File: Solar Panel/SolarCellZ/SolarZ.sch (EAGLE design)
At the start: 34 parts, among them X1 BU-SMA-V

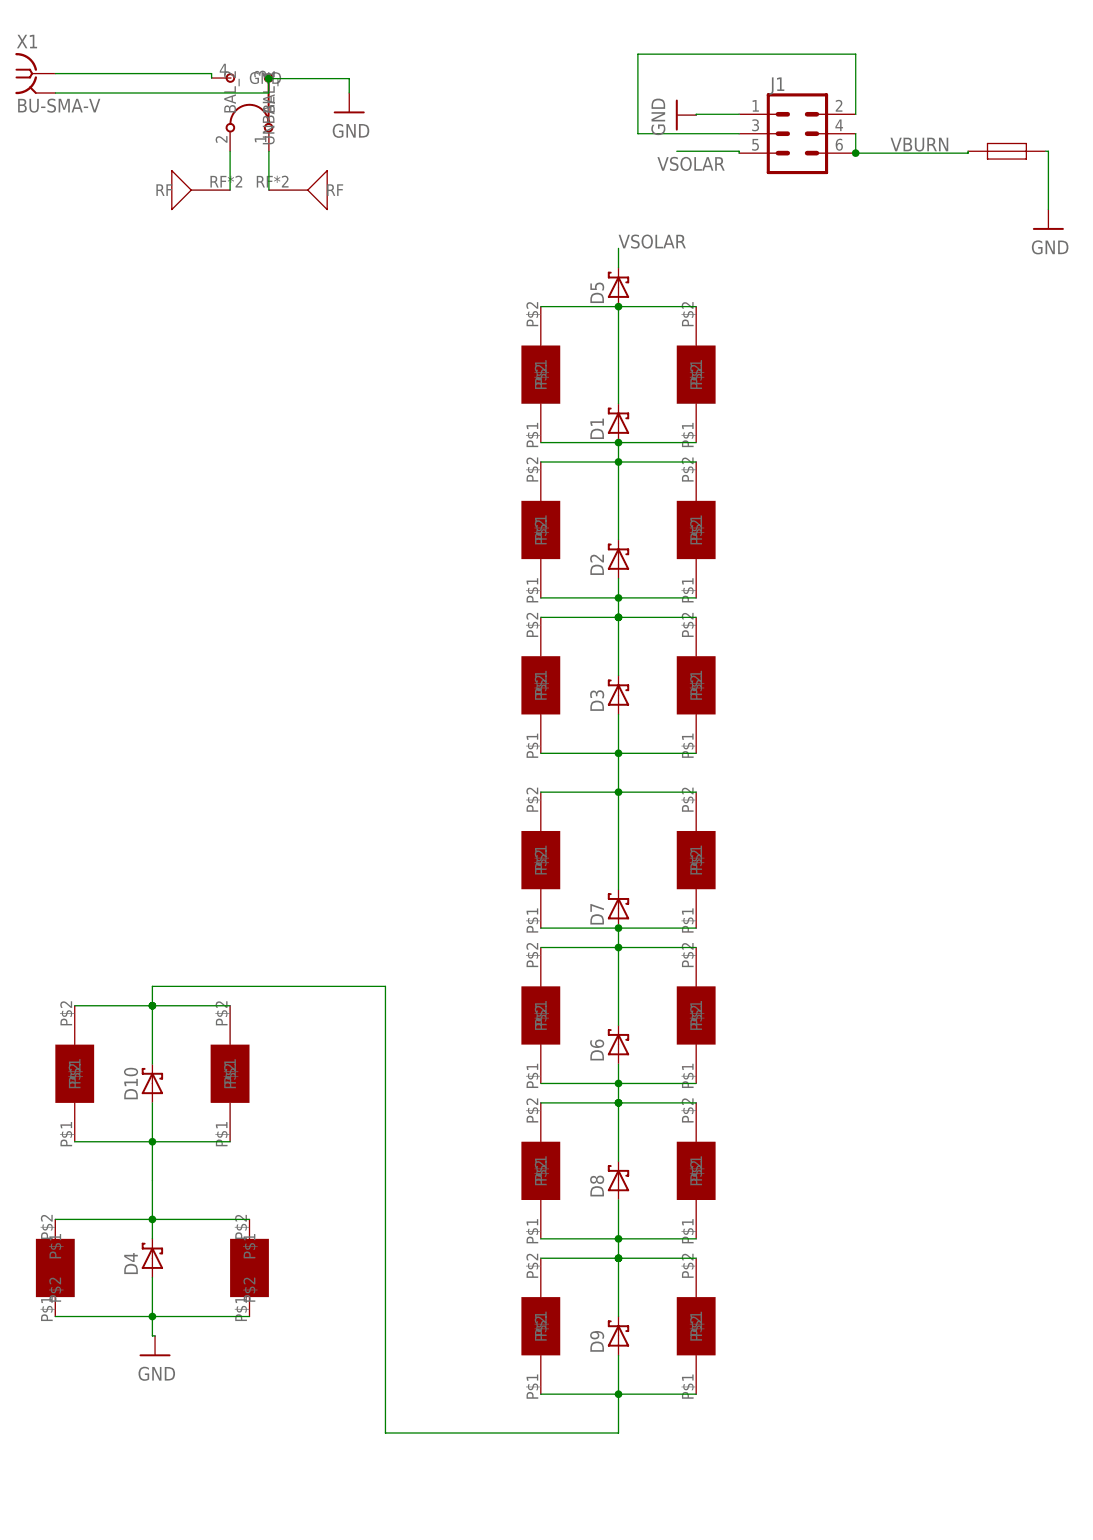
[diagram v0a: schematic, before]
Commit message: Routing on draft Z panel - dimensions need to be confirmed
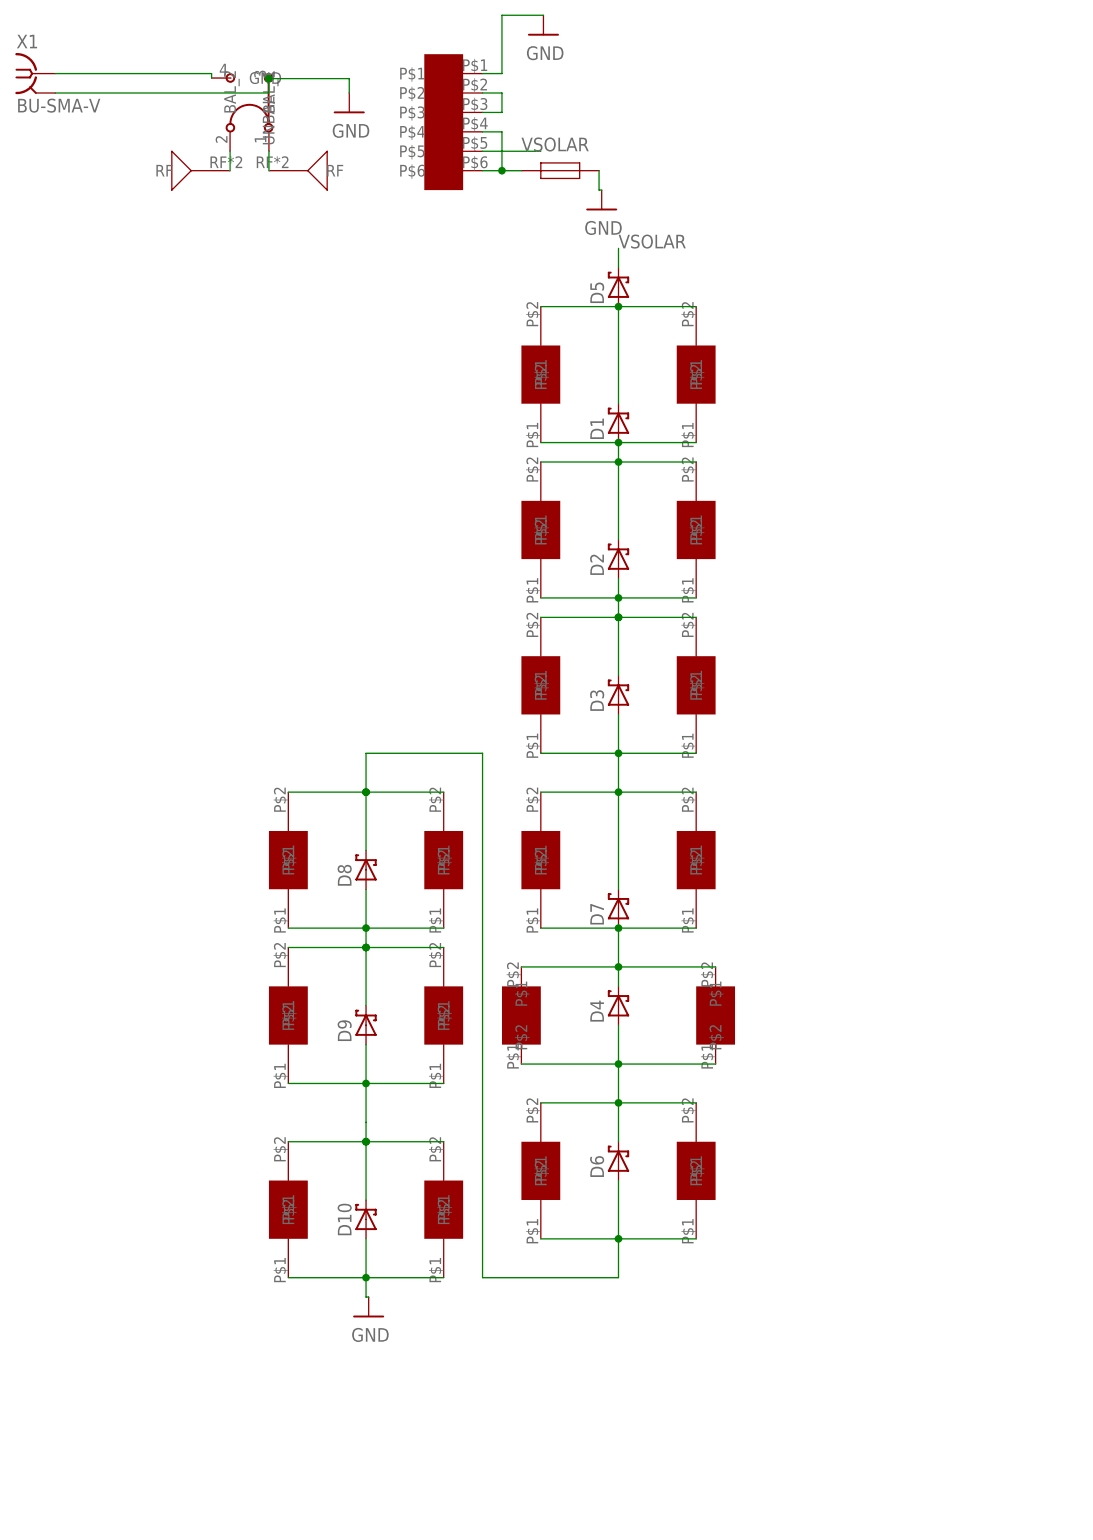
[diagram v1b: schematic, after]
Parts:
- removed F1: (no value), pandasat:BURN_TERM
- removed J1: (no value), pandasat:CONN_03X22X3_SILK_MALE_PTH
- added F2: (no value), pandasat:BURN_TERM
- added U$4: M20-8760342, Solar:M20-8760342
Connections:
- removed net N$1 (its old number): J1.2, J1.3
- removed net N$13: 17.P$1, 18.P$1, D10.POS
- removed net N$4: U$1.BAL_2, U$2.RF
- removed net N$5: U$1.BAL_1, U$3.RF
- removed net VBURN: F1.1, J1.4, J1.6
- new net N$16: F2.1, U$4.P$4, U$4.P$6
- new net N$8: U$4.P$2, U$4.P$3
- new net N$9: 10.P$1, 11.P$1, 6.P$2, 7.P$2, D4.NEG, D7.POS
- new net RF_P: U$1.BAL_2, U$3.RF
- net GND: now also 17.P$1, 18.P$1, D10.POS, F2.2, U$4.P$1; no longer 6.P$1, 7.P$1, D4.POS, F1.2, J1.1
- net N$11: now also 6.P$1, 7.P$1, D4.POS; no longer 10.P$1, 11.P$1, D7.POS
- net N$3: now also U$1.BAL_1, U$2.RF; no longer 6.P$2, 7.P$2, D4.NEG
- net VSOLAR: now also U$4.P$5; no longer J1.5
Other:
- moved on the sheet: D10, D4, D6, D8, D9

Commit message: Some Magnetorquer routing
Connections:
- removed net RF_P: U$1.BAL_2, U$3.RF
- new net N$4: U$1.BAL_1, U$3.RF
- net N$3: now also U$1.BAL_2; no longer U$1.BAL_1
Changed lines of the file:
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@@
 </instance>
 <instance part="U$1" gate="G$1" x="50.8" y="187.96" smashed="yes" rot="R180"/>
-<instance part="U$2" gate="G$1" x="58.42" y="180.34" smashed="yes" rot="R270"/>
-<instance part="U$3" gate="G$1" x="43.18" y="180.34" smashed="yes" rot="R90"/>
+<instance part="U$2" gate="G$1" x="43.18" y="180.34" smashed="yes" rot="R90"/>
+<instance part="U$3" gate="G$1" x="58.42" y="180.34" smashed="yes" rot="R270"/>
 <instance part="13" gate="G$1" x="91.44" y="137.16" smashed="yes" rot="R180"/>
 <instance part="D2" gate="G$1" x="99.06" y="129.54" smashed="yes" rot="R90">
@@
 <net name="N$3" class="0">
 <segment>
+<pinref part="U$1" gate="G$1" pin="BAL_2"/>
+<pinref part="U$2" gate="G$1" pin="RF"/>
+<wire x1="48.26" y1="182.88" x2="48.26" y2="180.34" width="0.1524" layer="91"/>
+</segment>
+</net>
+<net name="N$4" class="0">
+<segment>
 <pinref part="U$1" gate="G$1" pin="BAL_1"/>
-<pinref part="U$2" gate="G$1" pin="RF"/>
+<pinref part="U$3" gate="G$1" pin="RF"/>
 <wire x1="53.34" y1="182.88" x2="53.34" y2="180.34" width="0.1524" layer="91"/>
 </segment>
 </net>
-<net name="RF_P" class="0">
-<segment>
-<pinref part="U$1" gate="G$1" pin="BAL_2"/>
-<pinref part="U$3" gate="G$1" pin="RF"/>
-<wire x1="48.26" y1="182.88" x2="48.26" y2="180.34" width="0.1524" layer="91"/>
-</segment>
-</net>

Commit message: Magnetorquers done
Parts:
- removed 15, 16, 17, 18: KXOB22-04X3F, Solar:KXOB22-04X3F
- removed D10, D9: SB_DIODE, Solar:SB_DIODE
- added F1: (no value), pandasat:BURN_TERM
- 12, 14, 2, 3, 4, 5, 8, 9: value KXOB22-04X3F -> SLMD121H04L; device Solar:KXOB22-04X3F -> Solar:SLMD121H04L
- 6, 7: value SLMD121H04L -> KXOB22-04X3F; device Solar:SLMD121H04L -> Solar:KXOB22-04X3F
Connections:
- removed net N$14: 12.P$1, 14.P$1, 15.P$2, 16.P$2, D8.POS, D9.NEG
- removed net N$18: 12.P$2, 14.P$2, 8.P$1, 9.P$1, D6.POS, D8.NEG
- removed net N$4: U$1.BAL_1, U$3.RF
- new net N8: 12.P$1, 14.P$1, 6.P$2, 7.P$2, D4.NEG, D8.POS
- net GND: now also 8.P$1, 9.P$1, D6.POS, F1.2; no longer 17.P$1, 18.P$1, D10.POS
- net N$1: now also U$1.BAL_2, U$3.RF; no longer 15.P$1, 16.P$1, 17.P$2, 18.P$2, D10.NEG, D9.POS
- net N$16: now also F1.1
- net N$3: now also U$1.BAL_1; no longer U$1.BAL_2
- net N$9: now also 12.P$2, 14.P$2, D8.NEG; no longer 6.P$2, 7.P$2, D4.NEG
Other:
- moved on the sheet: D1, D4, D6, D7, D8
